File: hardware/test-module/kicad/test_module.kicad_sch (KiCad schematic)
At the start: 14 parts, among them J1 Barrel_Jack_12V, M1 ERM_Motor, M2 Stepper_4wire, M3 Servo_3pin, U1 D24V22F5_Buck, U2 Pi_Pico_W, U3 DRV2605L_Breakout, U4 DRV8871_Breakout, U5 DRV8825_Carrier

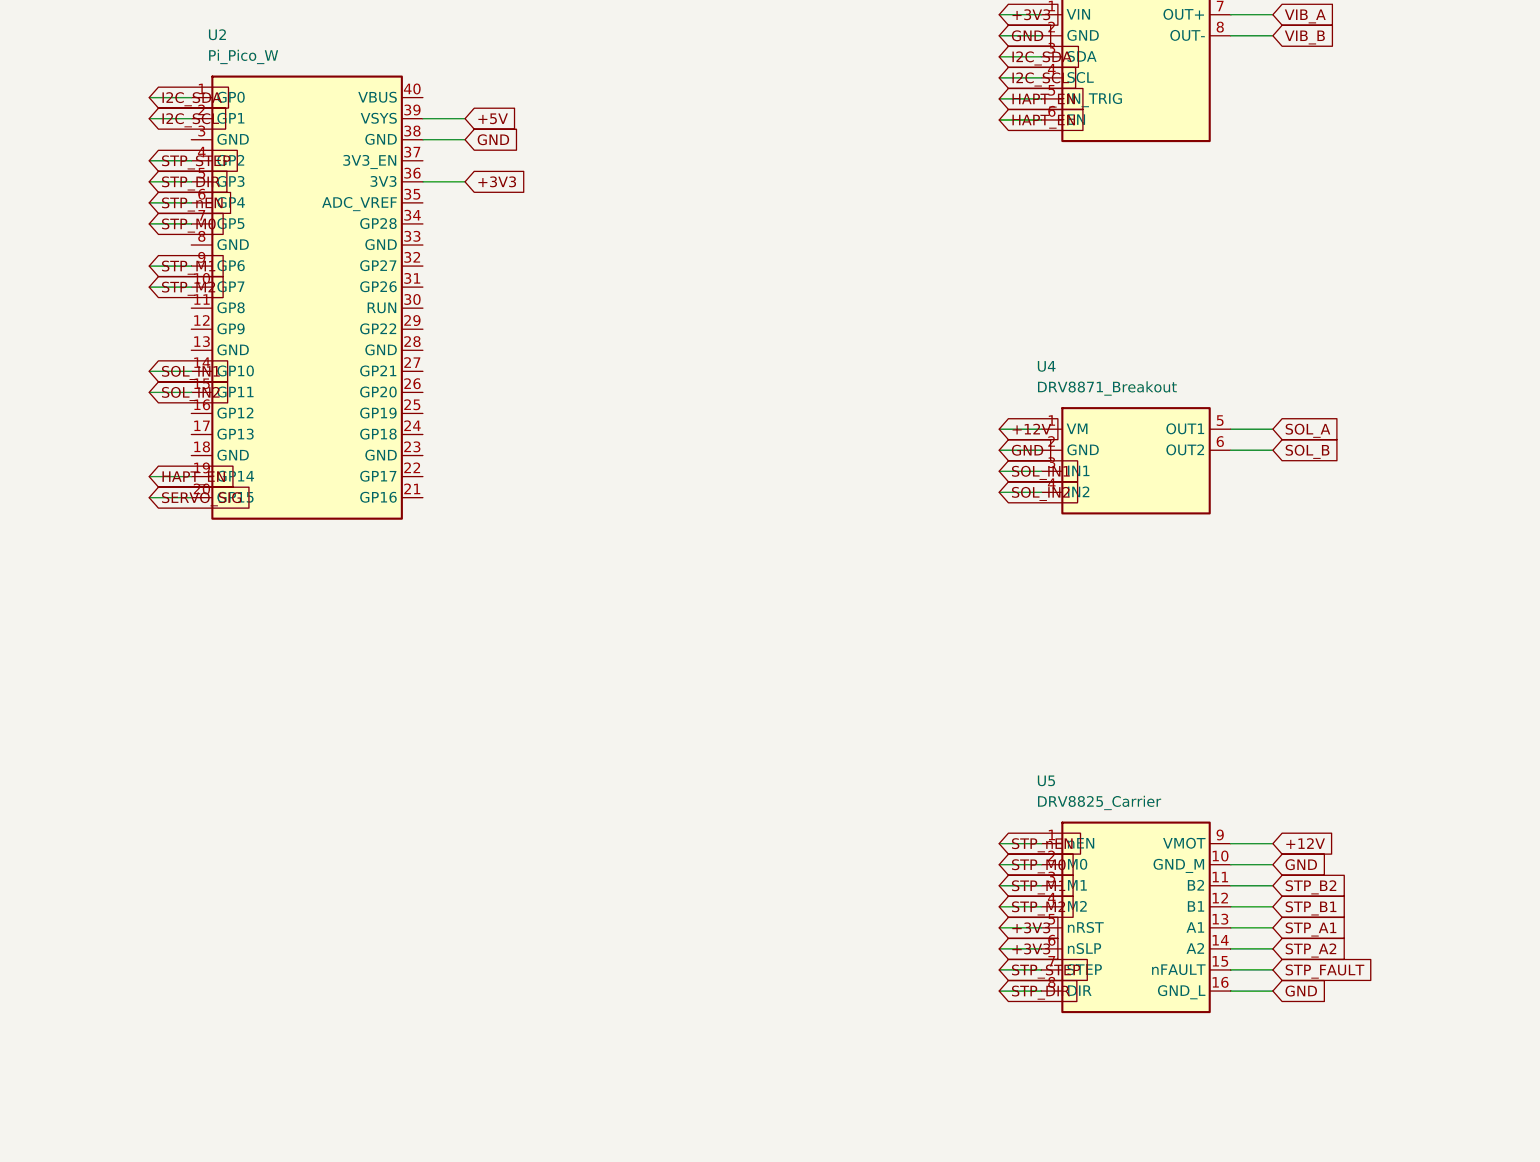
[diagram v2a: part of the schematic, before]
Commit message: Swap bench-rig stepper driver from DRV8825 to Pololu Tic T500
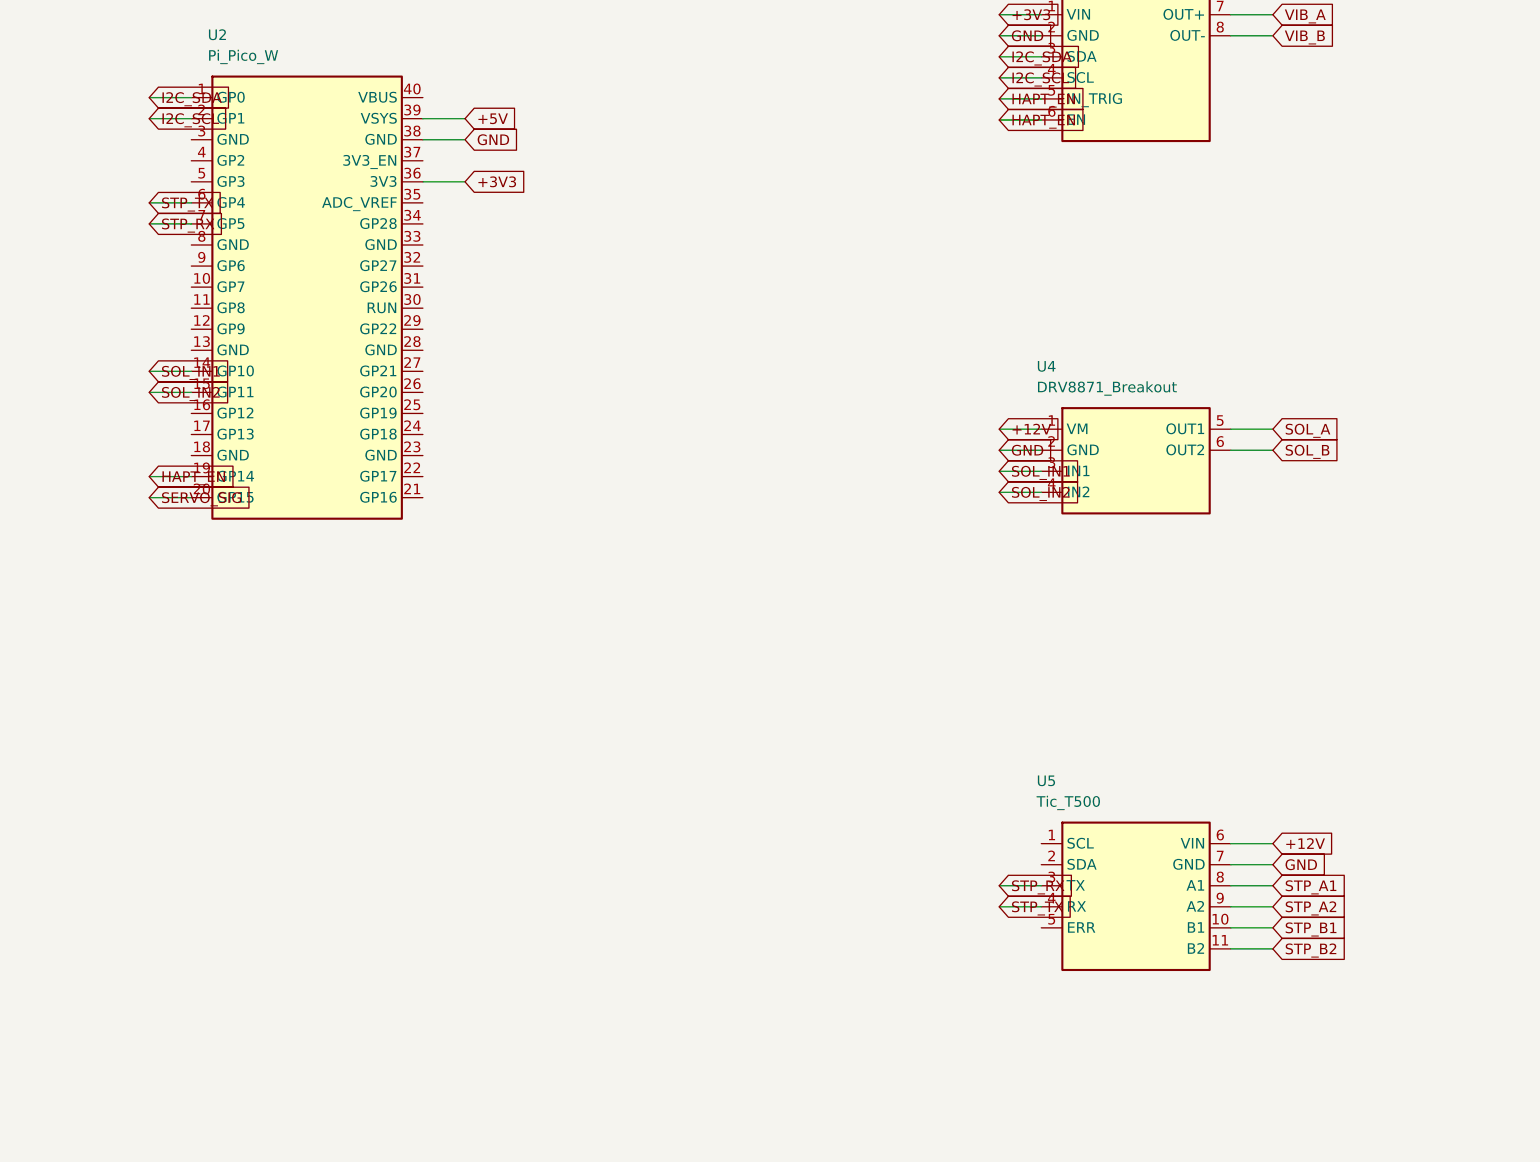
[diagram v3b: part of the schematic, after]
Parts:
- removed U5: DRV8825_Carrier, symbol test_module:DRV8825_Carrier
- added U5: Tic_T500, symbol test_module:Tic_T500
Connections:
- net +12V: now also U5.6 (VIN)
- net GND: now also U5.7 (GND)
- net STP_A1: now also U5.8 (A1)
- net STP_A2: now also U5.9 (A2)
- net STP_B1: now also U5.10 (B1)
- net STP_B2: now also U5.11 (B2)
- net STP_DIR: no longer names the net of U2.5 (GP3)
- net STP_M0 renamed STP_RX
- net STP_RX: now also U5.3 (TX)
- net STP_M1: no longer names the net of U2.9 (GP6)
- net STP_M2: no longer names the net of U2.10 (GP7)
- net STP_STEP: no longer names the net of U2.4 (GP2)
- net STP_nEN renamed STP_TX
- net STP_TX: now also U5.4 (RX)
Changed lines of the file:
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@@
-  (effects (font (size 1.27 1.27)) (justify left))
-)
-(wire (pts (xy 96.03 60.16) (xy 90.95 60.16))
-  (stroke (width 0) (type default)) (stroke (width 0) (type default))
-)
-(global_label "STP_STEP" (shape input) (at 90.95 60.16 180) (fields_autoplaced)
-  (effects (font (size 1.27 1.27)) (justify left))
-)
-(wire (pts (xy 96.03 62.7) (xy 90.95 62.7))
-  (stroke (width 0) (type default)) (stroke (width 0) (type default))
-)
-(global_label "STP_DIR" (shape input) (at 90.95 62.7 180) (fields_autoplaced)
   (effects (font (size 1.27 1.27)) (justify left))
 )
@@
   (stroke (width 0) (type default)) (stroke (width 0) (type default))
 )
-(global_label "STP_nEN" (shape input) (at 90.95 65.24 180) (fields_autoplaced)
+(global_label "STP_TX" (shape input) (at 90.95 65.24 180) (fields_autoplaced)
   (effects (font (size 1.27 1.27)) (justify left))
 )
@@
   (stroke (width 0) (type default)) (stroke (width 0) (type default))
 )
-(global_label "STP_M0" (shape input) (at 90.95 67.78 180) (fields_autoplaced)
-  (effects (font (size 1.27 1.27)) (justify left))
-)
-(wire (pts (xy 96.03 72.86) (xy 90.95 72.86))
-  (stroke (width 0) (type default)) (stroke (width 0) (type default))
-)
-(global_label "STP_M1" (shape input) (at 90.95 72.86 180) (fields_autoplaced)
-  (effects (font (size 1.27 1.27)) (justify left))
-)
-(wire (pts (xy 96.03 75.4) (xy 90.95 75.4))
-  (stroke (width 0) (type default)) (stroke (width 0) (type default))
-)
-(global_label "STP_M2" (shape input) (at 90.95 75.4 180) (fields_autoplaced)
+(global_label "STP_RX" (shape input) (at 90.95 67.78 180) (fields_autoplaced)
   (effects (font (size 1.27 1.27)) (justify left))
 )
@@
   (effects (font (size 1.27 1.27)) (justify left))
 )
-(symbol (lib_id "test_module:DRV8825_Carrier") (at 210 140 0) (unit 1)
+(symbol (lib_id "test_module:Tic_T500") (at 210 140 0) (unit 1)
   (in_bom yes) (on_board yes) (dnp no)
   (property "Reference" "U5" (id 0) (at 198 135 0)
     (effects (font (size 1.27 1.27)) (justify left)))
-  (property "Value" "DRV8825_Carrier" (id 1) (at 198 137.5 0)
+  (property "Value" "Tic_T500" (id 1) (at 198 137.5 0)
     (effects (font (size 1.27 1.27)) (justify left)))
   (property "Footprint" "" (id 2) (at 210 140 0)
@@
   )
 )
-(wire (pts (xy 198.57 157.78) (xy 193.48999999999998 157.78))
-  (stroke (width 0) (type default)) (stroke (width 0) (type default))
-)
-(global_label "STP_STEP" (shape input) (at 193.48999999999998 157.78 180) (fields_autoplaced)
-  (effects (font (size 1.27 1.27)) (justify left))
-)
-(wire (pts (xy 198.57 160.32) (xy 193.48999999999998 160.32))
-  (stroke (width 0) (type default)) (stroke (width 0) (type default))
-)
-(global_label "STP_DIR" (shape input) (at 193.48999999999998 160.32 180) (fields_autoplaced)
-  (effects (font (size 1.27 1.27)) (justify left))
-)
-(wire (pts (xy 198.57 142.54) (xy 193.48999999999998 142.54))
-  (stroke (width 0) (type default)) (stroke (width 0) (type default))
-)
-(global_label "STP_nEN" (shape input) (at 193.48999999999998 142.54 180) (fields_autoplaced)
-  (effects (font (size 1.27 1.27)) (justify left))
-)
-(wire (pts (xy 198.57 155.24) (xy 193.48999999999998 155.24))
-  (stroke (width 0) (type default)) (stroke (width 0) (type default))
-)
-(global_label "+3V3" (shape input) (at 193.48999999999998 155.24 180) (fields_autoplaced)
-  (effects (font (size 1.27 1.27)) (justify left))
-)
-(wire (pts (xy 198.57 152.7) (xy 193.48999999999998 152.7))
-  (stroke (width 0) (type default)) (stroke (width 0) (type default))
-)
-(global_label "+3V3" (shape input) (at 193.48999999999998 152.7 180) (fields_autoplaced)
-  (effects (font (size 1.27 1.27)) (justify left))
-)
-(wire (pts (xy 198.57 145.08) (xy 193.48999999999998 145.08))
-  (stroke (width 0) (type default)) (stroke (width 0) (type default))
-)
-(global_label "STP_M0" (shape input) (at 193.48999999999998 145.08 180) (fields_autoplaced)
+(wire (pts (xy 198.57 150.16) (xy 193.48999999999998 150.16))
+  (stroke (width 0) (type default)) (stroke (width 0) (type default))
+)
+(global_label "STP_TX" (shape input) (at 193.48999999999998 150.16 180) (fields_autoplaced)
   (effects (font (size 1.27 1.27)) (justify left))
 )
@@
   (stroke (width 0) (type default)) (stroke (width 0) (type default))
 )
-(global_label "STP_M1" (shape input) (at 193.48999999999998 147.62 180) (fields_autoplaced)
-  (effects (font (size 1.27 1.27)) (justify left))
-)
-(wire (pts (xy 198.57 150.16) (xy 193.48999999999998 150.16))
-  (stroke (width 0) (type default)) (stroke (width 0) (type default))
-)
-(global_label "STP_M2" (shape input) (at 193.48999999999998 150.16 180) (fields_autoplaced)
-  (effects (font (size 1.27 1.27)) (justify left))
-)
-(wire (pts (xy 221.43 157.78) (xy 226.51000000000002 157.78))
-  (stroke (width 0) (type default)) (stroke (width 0) (type default))
-)
-(global_label "STP_FAULT" (shape input) (at 226.51000000000002 157.78 0) (fields_autoplaced)
+(global_label "STP_RX" (shape input) (at 193.48999999999998 147.62 180) (fields_autoplaced)
   (effects (font (size 1.27 1.27)) (justify left))
 )
@@
   (effects (font (size 1.27 1.27)) (justify left))
 )
-(wire (pts (xy 221.43 160.32) (xy 226.51000000000002 160.32))
-  (stroke (width 0) (type default)) (stroke (width 0) (type default))
-)
-(global_label "GND" (shape input) (at 226.51000000000002 160.32 0) (fields_autoplaced)
+(wire (pts (xy 221.43 147.62) (xy 226.51000000000002 147.62))
+  (stroke (width 0) (type default)) (stroke (width 0) (type default))
+)
+(global_label "STP_A1" (shape input) (at 226.51000000000002 147.62 0) (fields_autoplaced)
+  (effects (font (size 1.27 1.27)) (justify left))
+)
+(wire (pts (xy 221.43 150.16) (xy 226.51000000000002 150.16))
+  (stroke (width 0) (type default)) (stroke (width 0) (type default))
+)
+(global_label "STP_A2" (shape input) (at 226.51000000000002 150.16 0) (fields_autoplaced)
   (effects (font (size 1.27 1.27)) (justify left))
 )
@@
   (stroke (width 0) (type default)) (stroke (width 0) (type default))
 )
-(global_label "STP_A1" (shape input) (at 226.51000000000002 152.7 0) (fields_autoplaced)
+(global_label "STP_B1" (shape input) (at 226.51000000000002 152.7 0) (fields_autoplaced)
   (effects (font (size 1.27 1.27)) (justify left))
 )
@@
   (stroke (width 0) (type default)) (stroke (width 0) (type default))
 )
-(global_label "STP_A2" (shape input) (at 226.51000000000002 155.24 0) (fields_autoplaced)
-  (effects (font (size 1.27 1.27)) (justify left))
-)
-(wire (pts (xy 221.43 150.16) (xy 226.51000000000002 150.16))
-  (stroke (width 0) (type default)) (stroke (width 0) (type default))
-)
-(global_label "STP_B1" (shape input) (at 226.51000000000002 150.16 0) (fields_autoplaced)
-  (effects (font (size 1.27 1.27)) (justify left))
-)
-(wire (pts (xy 221.43 147.62) (xy 226.51000000000002 147.62))
-  (stroke (width 0) (type default)) (stroke (width 0) (type default))
-)
-(global_label "STP_B2" (shape input) (at 226.51000000000002 147.62 0) (fields_autoplaced)
-  (effects (font (size 1.27 1.27)) (justify left))
-)
+(global_label "STP_B2" (shape input) (at 226.51000000000002 155.24 0) (fields_autoplaced)
+  (effects (font (size 1.27 1.27)) (justify left))
+)
